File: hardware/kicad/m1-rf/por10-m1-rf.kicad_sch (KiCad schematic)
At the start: 9 parts, among them U1 Si4735-D60-SSOP24, X1 32.768kHz

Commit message: M1.3: move ferrite connector into qualified schematic root
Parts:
- added J_AM_FERRITE: FERRITE_LOOPSTICK, symbol Connector_Generic:Conn_01x02
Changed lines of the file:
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@@
     (instances (project "por10-m1-rf" (path "/2b0f5db7-74f4-4a9a-bfc8-7bcbf6f10a13" (reference "TP_AMI") (unit 1))))
   )
-  (sheet_instances
-    (path "/" (page "1"))
-  )
-)
-		(wire (pts (xy 139.7 96.52) (xy 143.51 96.52)) (stroke (width 0) (type default)))
-	(wire (pts (xy 114.3 109.22) (xy 111.76 109.22) (xy 111.76 116.84) (xy 151.13 116.84) (xy 151.13 96.52)) (stroke (width 0) (type default)))
-  (symbol
+(symbol
     (lib_id "Connector_Generic:Conn_01x02")
     (at 106.68 106.68 0)
@@
     (instances (project "por10-m1-rf" (path "/2b0f5db7-74f4-4a9a-bfc8-7bcbf6f10a13" (reference "J_AM_FERRITE") (unit 1))))
   )
+  (sheet_instances
+    (path "/" (page "1"))
+  )
+)
+		(wire (pts (xy 139.7 96.52) (xy 143.51 96.52)) (stroke (width 0) (type default)))
+	(wire (pts (xy 114.3 109.22) (xy 111.76 109.22) (xy 111.76 116.84) (xy 151.13 116.84) (xy 151.13 96.52)) (stroke (width 0) (type default)))

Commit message: M1.3: recapture Si4735 crystal signal wiring
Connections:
- net GND: now also C5.2, C6.2, U1.16 (SEN), U1.19 (RCLK), X1.1, X1.2
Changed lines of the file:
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@@
     (instances (project "por10-m1-rf" (path "/2b0f5db7-74f4-4a9a-bfc8-7bcbf6f10a13" (reference "J_AM_FERRITE") (unit 1))))
   )
+  (wire (pts (xy 114.3 109.22) (xy 123.19 109.22) (xy 123.19 104.14)) (stroke (width 0) (type default)))
+  (wire (pts (xy 123.19 104.14) (xy 143.51 104.14)) (stroke (width 0) (type default)))
+  (wire (pts (xy 130.81 104.14) (xy 139.7 104.14) (xy 139.7 96.52)) (stroke (width 0) (type default)))
+  (wire (pts (xy 130.81 104.14) (xy 151.13 104.14)) (stroke (width 0) (type default)))
   (sheet_instances
     (path "/" (page "1"))
   )
 )
-		(wire (pts (xy 139.7 96.52) (xy 143.51 96.52)) (stroke (width 0) (type default)))
-	(wire (pts (xy 114.3 109.22) (xy 111.76 109.22) (xy 111.76 116.84) (xy 151.13 116.84) (xy 151.13 96.52)) (stroke (width 0) (type default)))

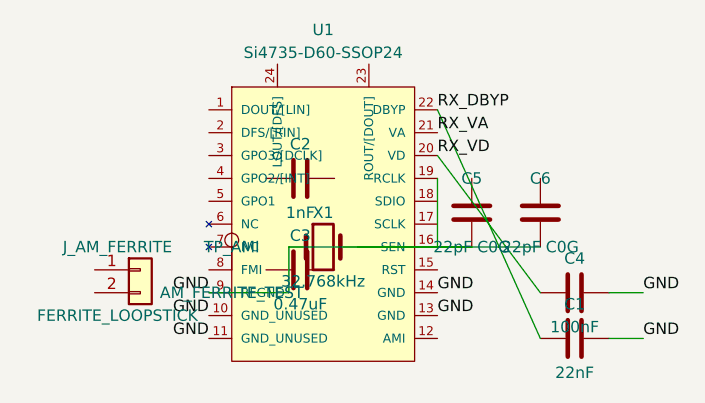
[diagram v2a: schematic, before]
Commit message: M1.3: revert malformed crystal wire capture
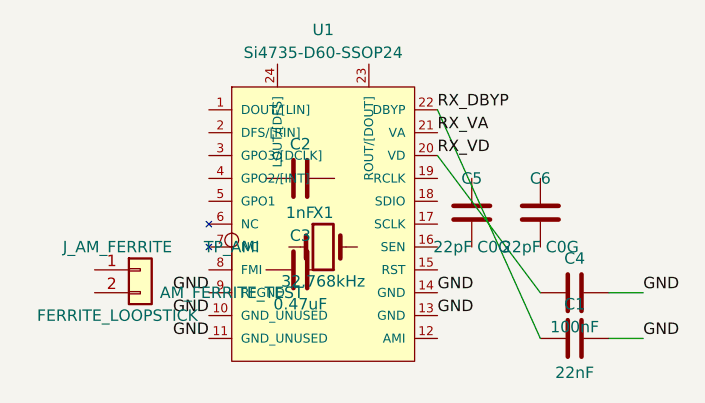
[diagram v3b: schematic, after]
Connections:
- net GND: no longer C5.2, C6.2, U1.16 (SEN), U1.19 (RCLK), X1.1, X1.2
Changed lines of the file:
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@@
     (instances (project "por10-m1-rf" (path "/2b0f5db7-74f4-4a9a-bfc8-7bcbf6f10a13" (reference "J_AM_FERRITE") (unit 1))))
   )
-  (wire (pts (xy 114.3 109.22) (xy 123.19 109.22) (xy 123.19 104.14)) (stroke (width 0) (type default)))
-  (wire (pts (xy 123.19 104.14) (xy 143.51 104.14)) (stroke (width 0) (type default)))
-  (wire (pts (xy 130.81 104.14) (xy 139.7 104.14) (xy 139.7 96.52)) (stroke (width 0) (type default)))
-  (wire (pts (xy 130.81 104.14) (xy 151.13 104.14)) (stroke (width 0) (type default)))
   (sheet_instances
     (path "/" (page "1"))

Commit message: M1.3: capture GPO3 to crystal node
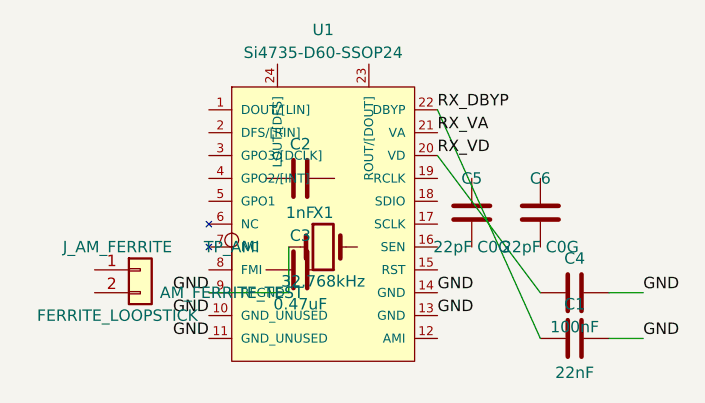
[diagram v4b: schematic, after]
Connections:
- net GND: now also X1.1
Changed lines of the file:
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@@
     (instances (project "por10-m1-rf" (path "/2b0f5db7-74f4-4a9a-bfc8-7bcbf6f10a13" (reference "J_AM_FERRITE") (unit 1))))
+  )
+  (wire
+    (pts
+      (xy 114.3 109.22) (xy 123.19 109.22) (xy 123.19 104.14)
+    )
+    (stroke
+      (width 0)
+      (type default)
+    )
   )
   (sheet_instances

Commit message: M1.3: simplify crystal wire to parser-known segment form
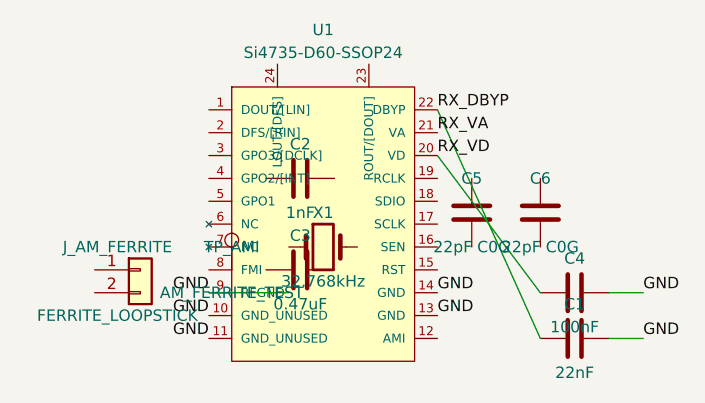
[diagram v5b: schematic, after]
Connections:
- net GND: no longer X1.1
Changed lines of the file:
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@@
     (instances (project "por10-m1-rf" (path "/2b0f5db7-74f4-4a9a-bfc8-7bcbf6f10a13" (reference "J_AM_FERRITE") (unit 1))))
   )
-  (wire
-    (pts
-      (xy 114.3 109.22) (xy 123.19 109.22) (xy 123.19 104.14)
-    )
-    (stroke
-      (width 0)
-      (type default)
-    )
-  )
+  (wire (pts (xy 114.3 109.22) (xy 123.19 109.22)) (stroke (width 0) (type default)))
   (sheet_instances
     (path "/" (page "1"))

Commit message: M1.3: connect GPO3 route to X1 pin 1
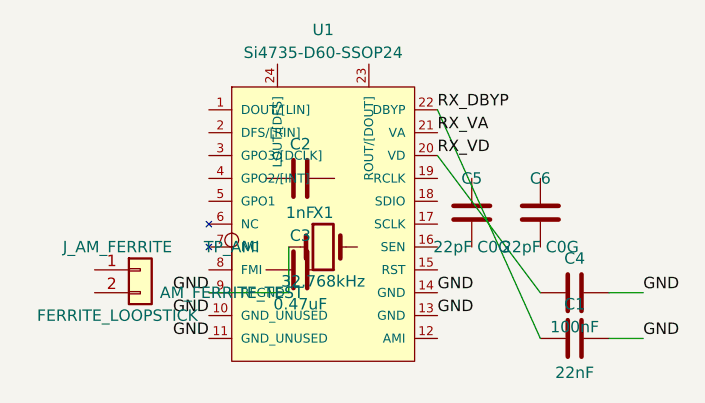
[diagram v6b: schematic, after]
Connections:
- net GND: now also X1.1
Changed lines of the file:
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@@
   )
   (wire (pts (xy 114.3 109.22) (xy 123.19 109.22)) (stroke (width 0) (type default)))
+  (wire (pts (xy 123.19 109.22) (xy 123.19 104.14)) (stroke (width 0) (type default)))
   (sheet_instances
     (path "/" (page "1"))

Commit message: M1.3: connect X1 pin 2 to RCLK
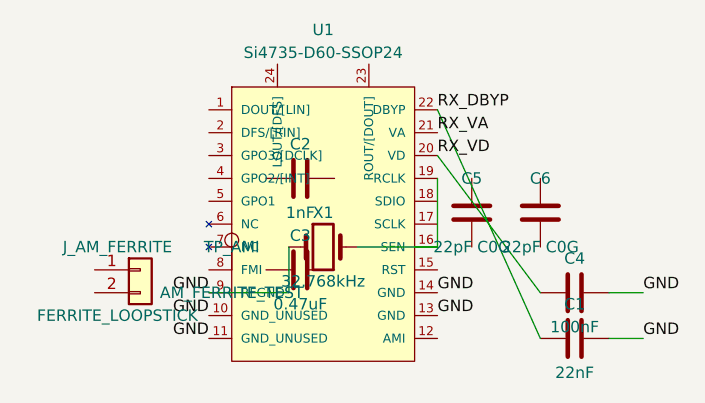
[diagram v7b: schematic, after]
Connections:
- net at X1.2: now also U1.16 (SEN), U1.19 (RCLK)
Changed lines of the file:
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@@
   (wire (pts (xy 114.3 109.22) (xy 123.19 109.22)) (stroke (width 0) (type default)))
   (wire (pts (xy 123.19 109.22) (xy 123.19 104.14)) (stroke (width 0) (type default)))
+  (wire (pts (xy 130.81 104.14) (xy 139.7 104.14)) (stroke (width 0) (type default)))
+  (wire (pts (xy 139.7 104.14) (xy 139.7 96.52)) (stroke (width 0) (type default)))
   (sheet_instances
     (path "/" (page "1"))

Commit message: M1.3: connect crystal load capacitor signal nodes
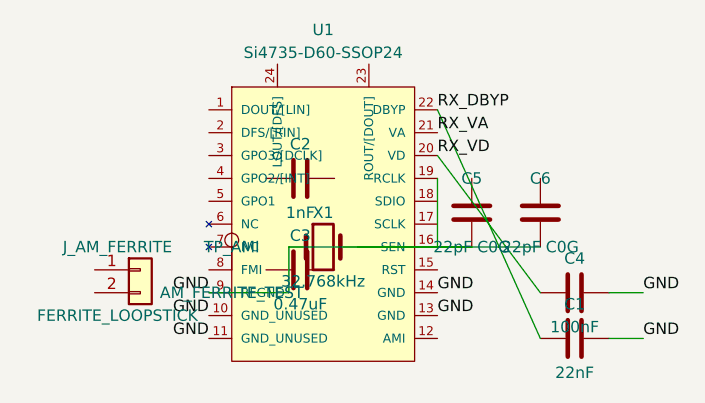
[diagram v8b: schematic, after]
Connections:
- net GND: now also C5.2, C6.2, U1.16 (SEN), U1.19 (RCLK), X1.2
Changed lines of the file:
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@@
   (wire (pts (xy 130.81 104.14) (xy 139.7 104.14)) (stroke (width 0) (type default)))
   (wire (pts (xy 139.7 104.14) (xy 139.7 96.52)) (stroke (width 0) (type default)))
+  (wire (pts (xy 123.19 104.14) (xy 143.51 104.14)) (stroke (width 0) (type default)))
+  (wire (pts (xy 130.81 104.14) (xy 151.13 104.14)) (stroke (width 0) (type default)))
   (sheet_instances
     (path "/" (page "1"))
